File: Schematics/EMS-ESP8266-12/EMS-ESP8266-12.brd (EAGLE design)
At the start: 75.9 x 48.2 mm, 43 parts, among them IC1 LM393N, T1 BC547B, T2 BC547B

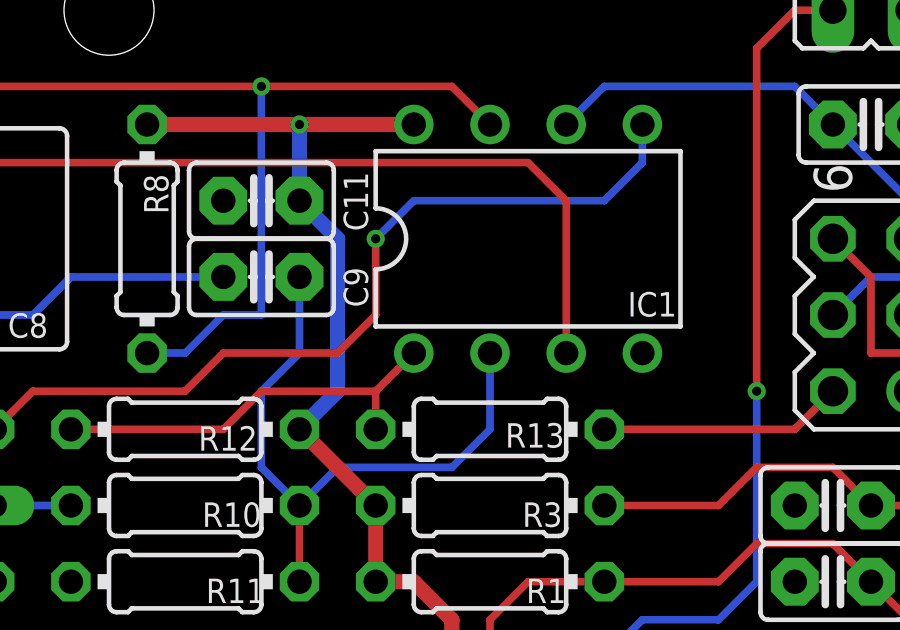
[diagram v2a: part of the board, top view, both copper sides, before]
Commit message: ESP8266/12 - Rev 1.0 - panelized for DirtyPCB - add descriptive Text to Layout and Headers / Jumpers
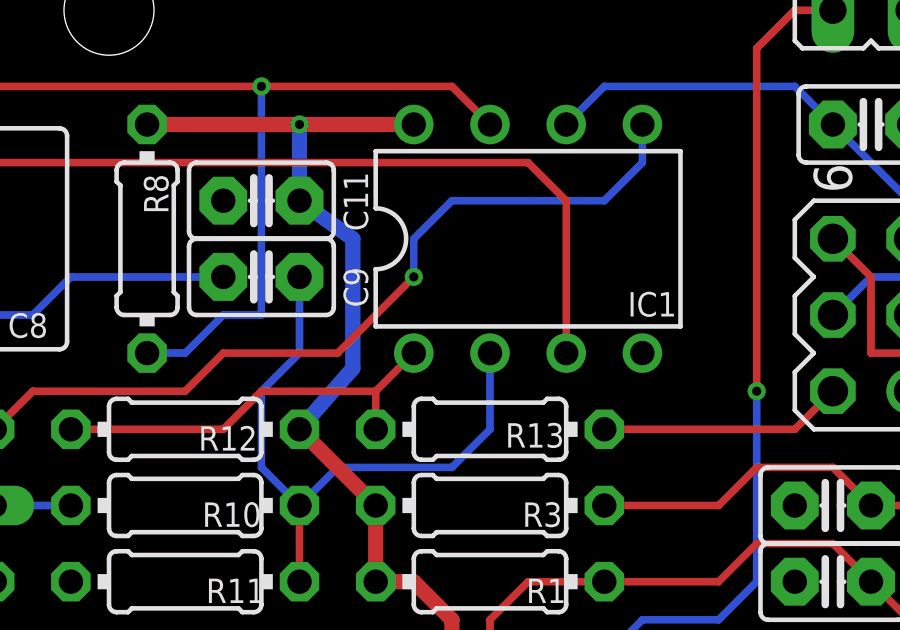
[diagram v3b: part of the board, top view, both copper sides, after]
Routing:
- net UREF: track 35.7 -> 34.9 mm
- net +3V3: track 60.8 -> 61.3 mm
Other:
- board text added: "C1"
- board text added: "C10"
- board text added: "C11"
- board text added: "C2"
- board text added: "C3"
- board text added: "C4"
- board text added: "C5"
- board text added: "C6"
- board text added: "C7"
- board text added: "C8"
- board text added: "C9"
- board text added: "D1"
- board text added: "D2"
- board text added: "D3"
- board text added: "D4"
- board text added: "D5"
- board text added: "D6"
- board text added: "EMS"
- board text added: "IC1"
- board text added: "L1"
- board text added: "L2"
- board text added: "LED1"
- board text added: "R1"
- board text added: "R10"
- board text added: "R11"
- board text added: "R12"
- board text added: "R13"
- board text added: "R2"
- board text added: "R3"
- board text added: "R4"
- board text added: "R5"
- board text added: "R6"
- board text added: "R7"
- board text added: "R8"
- board text added: "R9"
- board text added: "T1"
- board text added: "T2"
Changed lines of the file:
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@@
 <layer number="98" name="Guide" color="6" fill="1" visible="no" active="no"/>
 <layer number="99" name="SpiceOrder" color="5" fill="1" visible="no" active="no"/>
+<layer number="125" name="_tNames" color="14" fill="1" visible="yes" active="yes"/>
+<layer number="127" name="_tValues" color="14" fill="1" visible="no" active="yes"/>
 <layer number="200" name="200bmp" color="1" fill="10" visible="no" active="no"/>
 <layer number="250" name="Descript" color="7" fill="1" visible="yes" active="yes"/>
@@
 <hole x="34.29" y="45.72" drill="3"/>
 <hole x="15.24" y="2.54" drill="3"/>
-<text x="67.31" y="1.27" size="1.778" layer="16" rot="MR0">(c) JOr, 2015</text>
+<text x="67.31" y="1.27" size="1.778" layer="16" font="vector" rot="MR0">(c) JOr, 2015</text>
 <text x="69.215" y="31.75" size="1.27" layer="21" rot="R90">Program</text>
 <text x="64.135" y="34.29" size="1.27" layer="21" rot="R90">Mode</text>
@@
 <text x="74.93" y="24.13" size="1.27" layer="25" rot="R90">EMS-ESP12
 Rev 1.0</text>
+<text x="36.83" y="17.145" size="0.8128" layer="125">C1</text>
+<text x="61.214" y="27.432" size="0.8128" layer="125" ratio="10" rot="R270">C2</text>
+<text x="61.214" y="29.972" size="0.8128" layer="125" ratio="10" rot="R270">C3</text>
+<text x="22.86" y="3.81" size="0.8128" layer="125">C4</text>
+<text x="17.272" y="6.223" size="0.8128" layer="125" ratio="10" rot="R180">C5</text>
+<text x="35.56" y="3.81" size="0.8128" layer="125">C6</text>
+<text x="14.859" y="35.814" size="0.8128" layer="125" ratio="10">C7</text>
+<text x="32.258" y="35.61600625" size="0.8128" layer="125" ratio="10" rot="R180">C8</text>
+<text x="42.926" y="35.814" size="0.8128" layer="125" ratio="10" rot="R90">C9</text>
+<text x="63.246" y="40.894" size="0.8128" layer="125" ratio="10" rot="R90">C10</text>
+<text x="42.926" y="38.354" size="0.8128" layer="125" ratio="10" rot="R90">C11</text>
+<text x="13.335" y="15.494" size="0.8128" layer="125" ratio="10" rot="R90">D1</text>
+<text x="13.335" y="12.954" size="0.8128" layer="125" ratio="10" rot="R90">D2</text>
+<text x="13.335" y="18.034" size="0.8128" layer="125" ratio="10" rot="R90">D3</text>
+<text x="13.335" y="23.114" size="0.8128" layer="125" ratio="10" rot="R90">D4</text>
+<text x="13.335" y="20.574" size="0.8128" layer="125" ratio="10" rot="R90">D5</text>
+<text x="29.845" y="28.829" size="0.8128" layer="125" ratio="10" rot="R90">D6</text>
+<text x="11.392003125" y="2.3630875" size="1.27" layer="125" rot="R180">EMS</text>
+<text x="3.847996875" y="-0.6850125" size="1.27" layer="127">EMS</text>
+<text x="53.213" y="36.322" size="0.8128" layer="125" ratio="10" rot="R180">IC1</text>
+<text x="3.683" y="20.955" size="0.8128" layer="125" ratio="10" rot="R90">L1</text>
+<text x="2.921" y="38.481" size="0.8128" layer="125" ratio="10" rot="R270">L2</text>
+<text x="11.684" y="27.94" size="0.8128" layer="125" ratio="10" rot="R90">LED1</text>
+<text x="49.53" y="26.7716" size="0.8128" layer="125" ratio="10" rot="R180">R1</text>
+<text x="10.033" y="34.9504" size="0.8128" layer="125" ratio="10">R2</text>
+<text x="49.403" y="29.3116" size="0.8128" layer="125" ratio="10" rot="R180">R3</text>
+<text x="9.906" y="40.0304" size="0.8128" layer="125" ratio="10">R4</text>
+<text x="9.906" y="37.4904" size="0.8128" layer="125" ratio="10">R5</text>
+<text x="18.796" y="32.9946" size="0.8128" layer="125" ratio="10" rot="R180">R6</text>
+<text x="27.686" y="26.0604" size="0.8128" layer="125" ratio="10">R7</text>
+<text x="35.4584" y="40.259" size="0.8128" layer="125" ratio="10" rot="R270">R8</text>
+<text x="27.686" y="31.1404" size="0.8128" layer="125" ratio="10">R9</text>
+<text x="39.37" y="29.3116" size="0.8128" layer="125" ratio="10" rot="R180">R10</text>
+<text x="39.497" y="26.7716" size="0.8128" layer="125" ratio="10" rot="R180">R11</text>
+<text x="39.243" y="31.8516" size="0.8128" layer="125" ratio="10" rot="R180">R12</text>
+<text x="47.498" y="31.1404" size="0.8128" layer="125" ratio="10">R13</text>
+<text x="15.748" y="24.638" size="0.8128" layer="125" ratio="10" rot="R180">T1</text>
+<text x="20.193" y="36.068" size="0.8128" layer="125" ratio="10" rot="R180">T2</text>
 </plain>
 <attributes>
@@
 </variantdefs>
 <classes>
-<class number="0" name="default" width="0.254" drill="0">
+<class number="0" name="default" width="0.254" drill="0.2">
 <clearance class="0" value="0.254"/>
 </class>
-<class number="1" name="pwr" width="0.508" drill="0">
+<class number="1" name="pwr" width="0.508" drill="0.2">
+<clearance class="0" value="0.205"/>
 <clearance class="1" value="0.254"/>
 </class>
-<class number="2" name="signal" width="0.254" drill="0">
-<clearance class="2" value="0.1905"/>
+<class number="2" name="signal" width="0.254" drill="0.2">
+<clearance class="0" value="0.205"/>
+<clearance class="1" value="0.205"/>
+<clearance class="2" value="0.205"/>
 </class>
 </classes>
-<designrules name="dirt_cheap_dirty_boards.v1">
+<designrules name="EMS-ESP8266-12">
 <description language="en">&lt;b&gt;Dirty Cheap Dirty Board Design Rules&lt;/b&gt;
 &lt;br&gt;
@@
 <param name="mtCopper" value="0.035mm 0.0175mm 0.035mm 0.035mm 0.035mm 0.035mm 0.035mm 0.035mm 0.035mm 0.035mm 0.035mm 0.035mm 0.035mm 0.035mm 0.0175mm 0.035mm"/>
 <param name="mtIsolate" value="1.5mm 1.1mm 0.2mm 0.15mm 0.2mm 0.15mm 0.2mm 0.15mm 0.2mm 0.15mm 0.2mm 0.15mm 0.2mm 0.15mm 0.2mm"/>
-<param name="mdWireWire" value="5mil"/>
-<param name="mdWirePad" value="5mil"/>
-<param name="mdWireVia" value="5mil"/>
-<param name="mdPadPad" value="5mil"/>
-<param name="mdPadVia" value="5mil"/>
-<param name="mdViaVia" value="5mil"/>
+<param name="mdWireWire" value="0.205mm"/>
+<param name="mdWirePad" value="0.205mm"/>
+<param name="mdWireVia" value="0.205mm"/>
+<param name="mdPadPad" value="0.205mm"/>
+<param name="mdPadVia" value="0.205mm"/>
+<param name="mdViaVia" value="0.205mm"/>
 <param name="mdSmdPad" value="0mil"/>
 <param name="mdSmdVia" value="0mil"/>
@@
 <wire x1="52.07" y1="41.91" x2="52.07" y2="40.64" width="0.254" layer="16"/>
 <wire x1="52.07" y1="40.64" x2="50.8" y2="39.37" width="0.254" layer="16"/>
-<wire x1="50.8" y1="39.37" x2="44.45" y2="39.37" width="0.254" layer="16"/>
-<wire x1="44.45" y1="39.37" x2="43.18" y2="38.1" width="0.254" layer="16"/>
-<via x="43.18" y="38.1" extent="1-16" drill="0.3048" shape="octagon"/>
-<wire x1="43.18" y1="38.1" x2="43.18" y2="35.56" width="0.254" layer="1"/>
-<wire x1="43.18" y1="35.56" x2="41.91" y2="34.29" width="0.254" layer="1"/>
+<wire x1="50.8" y1="39.37" x2="45.72" y2="39.37" width="0.254" layer="16"/>
+<wire x1="45.72" y1="39.37" x2="44.45" y2="38.1" width="0.254" layer="16"/>
+<wire x1="44.45" y1="38.1" x2="44.45" y2="36.83" width="0.254" layer="16"/>
+<via x="44.45" y="36.83" extent="1-16" drill="0.3048" shape="octagon"/>
+<wire x1="44.45" y1="36.83" x2="41.91" y2="34.29" width="0.254" layer="1"/>
 <wire x1="41.91" y1="34.29" x2="38.1" y2="34.29" width="0.254" layer="1"/>
 <wire x1="38.1" y1="34.29" x2="36.83" y2="33.02" width="0.254" layer="1"/>
@@
 <contactref element="MOD1" pad="GND"/>
 <contactref element="C2" pad="2"/>
-<polygon width="0.4064" layer="16">
+<polygon width="0.4064" layer="16" isolate="0.381">
 <vertex x="0" y="48.26"/>
 <vertex x="71.12" y="48.26"/>
@@
 <wire x1="43.18" y1="26.67" x2="44.45" y2="26.67" width="0.508" layer="1"/>
 <wire x1="40.64" y1="31.75" x2="43.18" y2="29.21" width="0.508" layer="1"/>
-<wire x1="40.64" y1="39.37" x2="41.91" y2="38.1" width="0.508" layer="16"/>
-<wire x1="41.91" y1="38.1" x2="41.91" y2="33.02" width="0.508" layer="16"/>
-<wire x1="41.91" y1="33.02" x2="40.64" y2="31.75" width="0.508" layer="16"/>
+<wire x1="40.64" y1="39.37" x2="42.418" y2="38.1" width="0.508" layer="16"/>
+<wire x1="42.418" y1="38.1" x2="42.418" y2="33.782" width="0.508" layer="16"/>
+<wire x1="42.418" y1="33.782" x2="40.64" y2="31.75" width="0.508" layer="16"/>
 <wire x1="35.56" y1="41.91" x2="40.64" y2="41.91" width="0.508" layer="1"/>
 <wire x1="40.64" y1="41.91" x2="44.45" y2="41.91" width="0.508" layer="1"/>

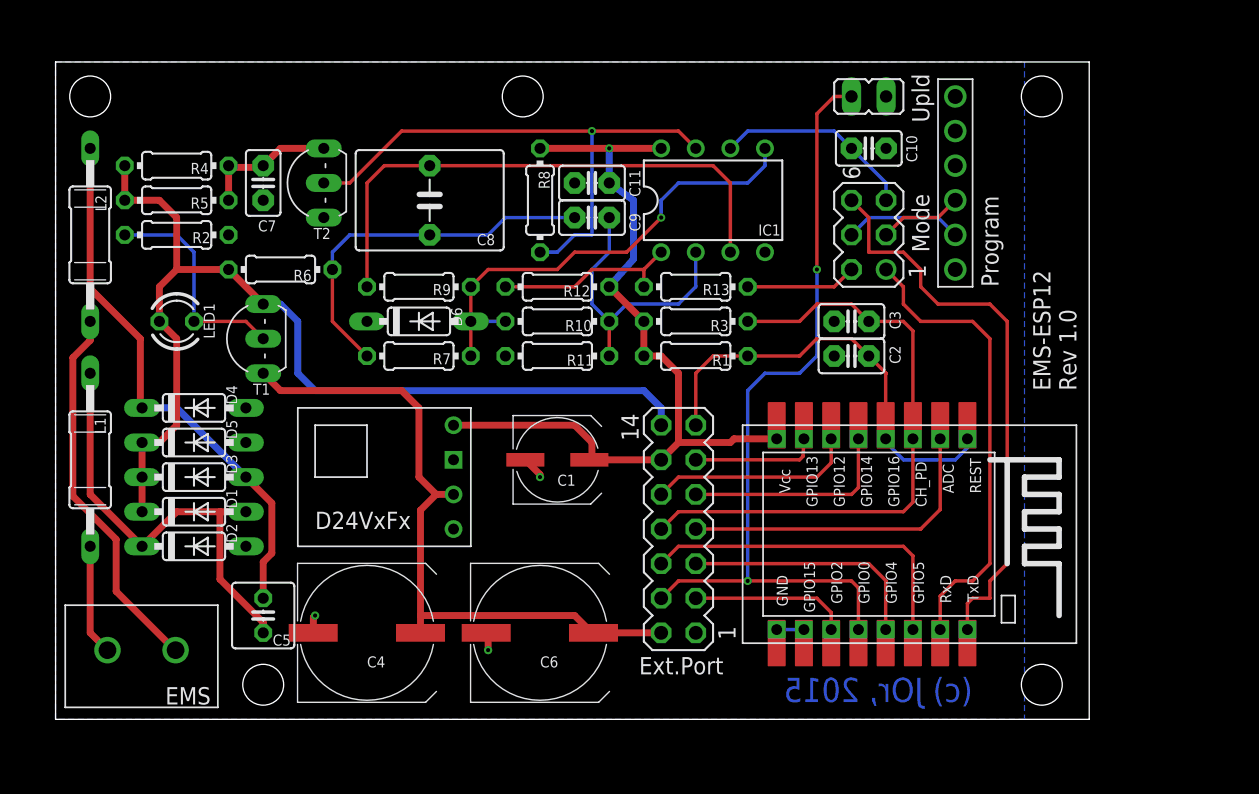
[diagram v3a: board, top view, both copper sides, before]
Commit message: Board Rev 1.0b - Ext. Port auf 16pin erweitert - GPIO15 auf Ext. Port gelegt - erfordert im Normalbetrieb einen  Jumper zw. Ext.Port, Pin 3-4 - Dummy Solder Jumper für Buck-Konverter /SHDN
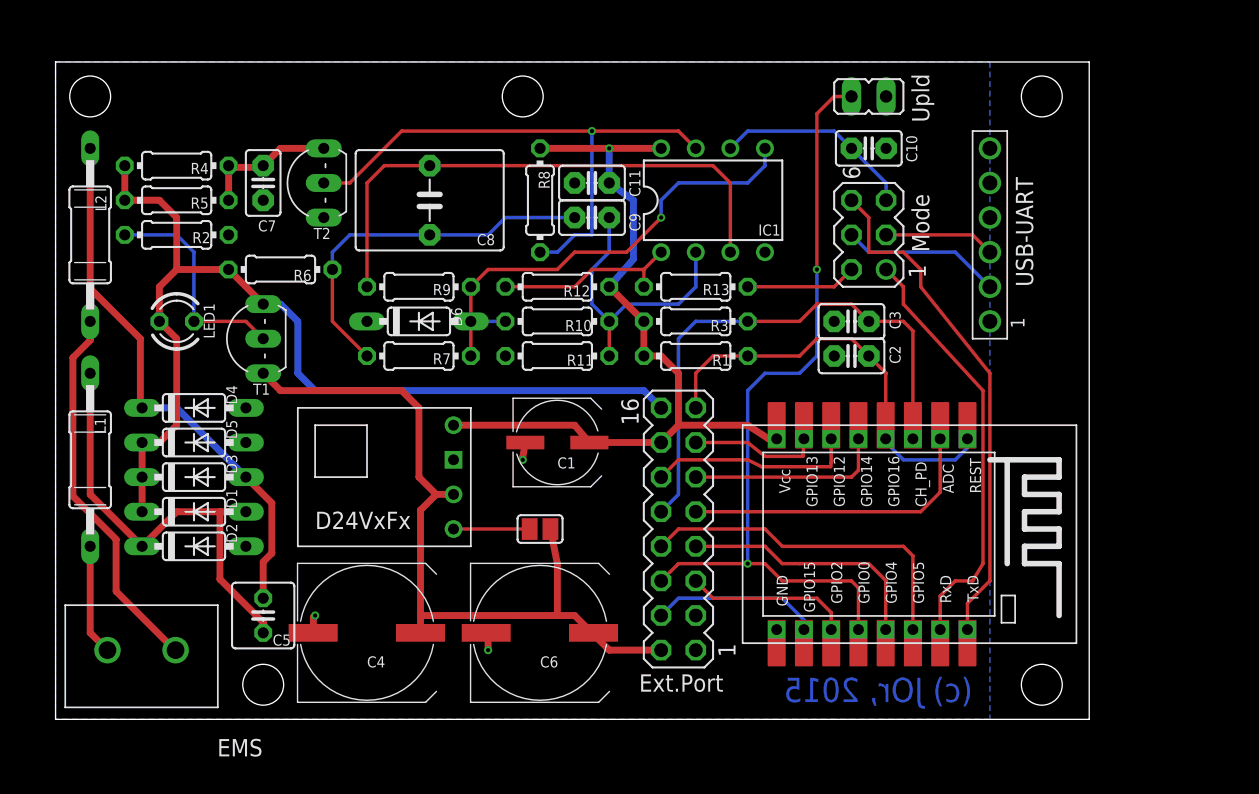
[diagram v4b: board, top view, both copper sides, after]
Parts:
- added SJ1: n.u., jumper:SJ
- EMS: value EMS -> 691102710002
- EXT.PORT: device con-lstb:MA07-2 -> con-lstb:MA08-2
- SV1: value (none) -> Mode
- moved PROGRAM 4.58 mm to (68.6, 35.6)
- moved C1 1.27 mm to (36.8, 20.3)
- renumbered MODE to SV1
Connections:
- new net N$3: MOD1./SHDN, SJ1.1
- net +3V3: now also EXT.PORT.14; no longer EXT.PORT.12
- net ADC: now also EXT.PORT.9; no longer EXT.PORT.7
- net CH_PD: now also EXT.PORT.10; no longer EXT.PORT.8
- net GND: now also ESP1.GND, EXT.PORT.3
- net GPIO0: now also EXT.PORT.6; no longer EXT.PORT.4
- net GPIO12: now also EXT.PORT.12; no longer EXT.PORT.10
- net GPIO13: now also EXT.PORT.13; no longer EXT.PORT.11
- net GPIO14: now also EXT.PORT.11; no longer EXT.PORT.9
- net GPIO15: now also EXT.PORT.4; no longer ESP1.GND
- net GPIO2: now also EXT.PORT.5; no longer EXT.PORT.3
- net GPIO4: now also EXT.PORT.7; no longer EXT.PORT.5
- net GPIO5: now also EXT.PORT.8; no longer EXT.PORT.6
- net REST: now also EXT.PORT.15; no longer EXT.PORT.13
- net UBUCK: now also SJ1.2
- net UEMS: now also EXT.PORT.16; no longer EXT.PORT.14
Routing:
- net GPIO15: track 2.00 -> 12.4 mm
- net UBUCK: track 49.5 -> 56.5 mm
- net N$3: track 0.00 -> 5.59 mm
- net CH_PD: track 45.3 -> 40.2 mm
- net UTXD: track 41.9 -> 37.6 mm
- net RXD: track 8.67 -> 11.7 mm
- net URXD: track 34.1 -> 31.2 mm
- net +3V3: track 61.3 -> 58.8 mm
- net TXD: track 6.13 -> 8.15 mm
- net REST: track 32.5 -> 31.2 mm
- net GPIO14: track 15.7 -> 14.5 mm
- net ADC: track 23.7 -> 22.5 mm
- net UEMS: track 74.6 -> 73.3 mm
- net GPIO0: track 59.2 -> 58.5 mm
- net GPIO5: track 24.7 -> 25.2 mm
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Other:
- board text added: "1"
- board text added: "EMS-ESP8266/12 Rev 1.0b"
- board text added: "USB-UART"
- board text removed: "EMS-ESP12 Rev 1.0"
- board text removed: "Program"
